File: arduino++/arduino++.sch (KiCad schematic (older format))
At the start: 23 parts, among them IC1 ATMEGA328PB-A, P1 CONN_01X18, P2 CONN_01X03, P3 USB_OTG, P4 CONN_01X03, P5 CONN_01X21, P6 CONN_01X03, P7 CONN_01X03, P8 CONN_02X03, Y1 Crystal

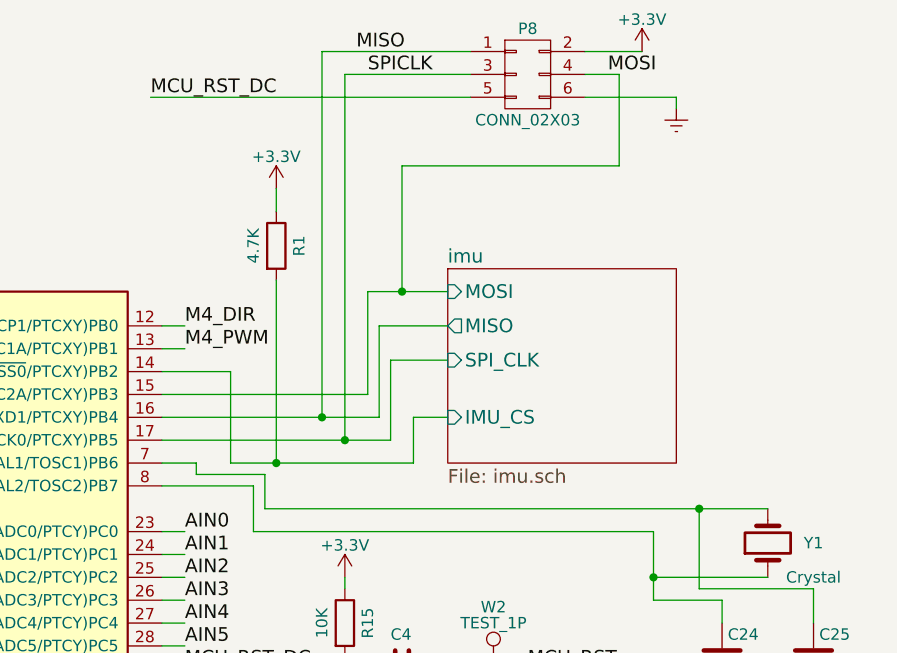
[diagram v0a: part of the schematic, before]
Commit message: Updating to latest rev as ordered on OSHPark.
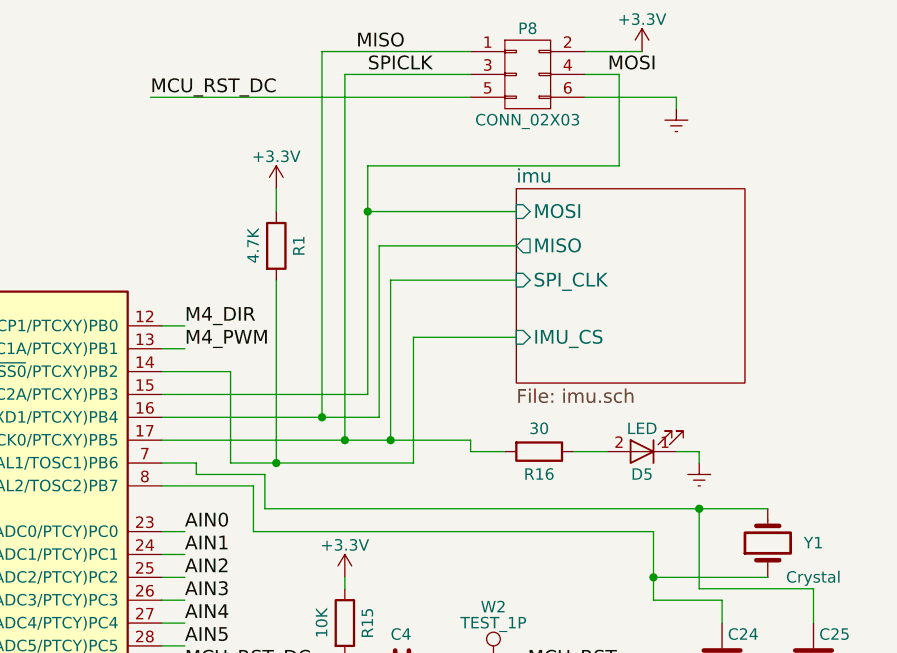
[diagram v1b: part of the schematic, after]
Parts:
- added D5: LED, LEDs:LED-0603, symbol LED
- added R16: 30, Resistors_SMD:R_0402, symbol R
- P3: manf# (none) -> 10118193-0001LF
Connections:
- net Earth: now also D5.1 (K)
- net SPICLK: now also R16.2
- new net: D5.2 (A), R16.1
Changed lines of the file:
@@
 F 2 "Connect:USB_Micro-B" H 4000 950 50  0001 C CNN
 F 3 "" V 4000 950 50  0000 C CNN
+F 4 "10118193-0001LF" H 4050 1050 60  0001 C CNN "manf#"
 	1    4050 1050
 	0    -1   -1   0
@@
 $EndComp
 $Comp
-L Earth #PWR01
+L Earth #PWR14
 U 1 1 582B5FCD
 P 4600 1500
-F 0 "#PWR01" H 4600 1250 50  0001 C CNN
+F 0 "#PWR14" H 4600 1250 50  0001 C CNN
 F 1 "Earth" H 4600 1350 50  0001 C CNN
 F 2 "" H 4600 1500 50  0000 C CNN
@@
 NoConn ~ 4350 950
 $Comp
-L Earth #PWR02
+L Earth #PWR16
 U 1 1 582B619C
 P 6000 5950
-F 0 "#PWR02" H 6000 5700 50  0001 C CNN
+F 0 "#PWR16" H 6000 5700 50  0001 C CNN
 F 1 "Earth" H 6000 5800 50  0001 C CNN
 F 2 "" H 6000 5950 50  0000 C CNN
@@
 $EndSheet
 $Sheet
-S 8700 2850 1000 850
+S 9000 2500 1000 850
 U 582C0B32
 F0 "imu" 60
 F1 "imu.sch" 60
-F2 "IMU_CS" I L 8700 3500 60
-F3 "SPI_CLK" I L 8700 3250 60
-F4 "MISO" O L 8700 3100 60
-F5 "MOSI" I L 8700 2950 60
+F2 "IMU_CS" I L 9000 3150 60
+F3 "SPI_CLK" I L 9000 2900 60
+F4 "MISO" O L 9000 2750 60
+F5 "MOSI" I L 9000 2600 60
 $EndSheet
 Text Label 7550 4000 0    60   ~ 0
@@
 $EndComp
 $Comp
-L Earth #PWR03
+L Earth #PWR13
 U 1 1 582C2BB8
 P 4550 3750
-F 0 "#PWR03" H 4550 3500 50  0001 C CNN
+F 0 "#PWR13" H 4550 3500 50  0001 C CNN
 F 1 "Earth" H 4550 3600 50  0001 C CNN
 F 2 "" H 4550 3750 50  0000 C CNN
@@
 M4_PWM
 $Comp
-L +3.3V #PWR04
+L +3.3V #PWR11
 U 1 1 582D1956
 P 3850 2650
-F 0 "#PWR04" H 3850 2500 50  0001 C CNN
+F 0 "#PWR11" H 3850 2500 50  0001 C CNN
 F 1 "+3.3V" H 3850 2790 50  0000 C CNN
 F 2 "" H 3850 2650 50  0000 C CNN
@@
 	4250 2950 4250 2950
 Wire Wire Line
-	7450 3600 8450 3600
+	7450 3600 8800 3600
 Wire Wire Line
 	7450 3500 8400 3500
 Wire Wire Line
-	7450 3400 8350 3400
+	8350 3400 7450 3400
 Wire Wire Line
 	7450 4000 7550 4000
@@
 Connection ~ 4550 3400
 Wire Wire Line
-	8350 3400 8350 2950
-Wire Wire Line
-	8350 2950 8700 2950
-Wire Wire Line
-	8400 3500 8400 3100
-Wire Wire Line
-	8400 3100 8700 3100
-Wire Wire Line
-	8450 3600 8450 3250
-Wire Wire Line
-	8450 3250 8700 3250
+	8350 2400 8350 3400
+Wire Wire Line
+	8350 2600 9000 2600
+Wire Wire Line
+	8400 3500 8400 2750
+Wire Wire Line
+	8400 2750 9000 2750
+Wire Wire Line
+	8450 3600 8450 2900
+Wire Wire Line
+	8450 2900 9000 2900
 Wire Wire Line
 	7750 3700 8550 3700
 Wire Wire Line
-	8550 3700 8550 3500
-Wire Wire Line
-	8550 3500 8700 3500
+	8550 3700 8550 3150
+Wire Wire Line
+	8550 3150 9000 3150
 Wire Wire Line
 	7950 3700 7950 2900
@@
 M4N
 $Comp
-L Earth #PWR05
+L Earth #PWR3
 U 1 1 58350D27
 P 1350 5150
-F 0 "#PWR05" H 1350 4900 50  0001 C CNN
+F 0 "#PWR3" H 1350 4900 50  0001 C CNN
 F 1 "Earth" H 1350 5000 50  0001 C CNN
 F 2 "" H 1350 5150 50  0000 C CNN
@@
 MCU_UART_TX
 $Comp
-L Earth #PWR06
+L Earth #PWR5
 U 1 1 58352CA7
 P 2600 5150
-F 0 "#PWR06" H 2600 4900 50  0001 C CNN
+F 0 "#PWR5" H 2600 4900 50  0001 C CNN
 F 1 "Earth" H 2600 5000 50  0001 C CNN
 F 2 "" H 2600 5150 50  0000 C CNN
@@
 M4_PWM
 $Comp
-L +3.3V #PWR07
+L +3.3V #PWR10
 U 1 1 5835EB7A
 P 3700 4950
-F 0 "#PWR07" H 3700 4800 50  0001 C CNN
+F 0 "#PWR10" H 3700 4800 50  0001 C CNN
 F 1 "+3.3V" H 3700 5090 50  0000 C CNN
 F 2 "" H 3700 4950 50  0000 C CNN
@@
 	7600 3700 7600 3750
 $Comp
-L +BATT #PWR08
+L +BATT #PWR4
 U 1 1 5836512B
 P 1700 4900
-F 0 "#PWR08" H 1700 4750 50  0001 C CNN
+F 0 "#PWR4" H 1700 4750 50  0001 C CNN
 F 1 "+BATT" H 1700 5040 50  0000 C CNN
 F 2 "" H 1700 4900 50  0000 C CNN
@@
 	3550 1350 4600 1350
 $Comp
-L PWR_FLAG #FLG09
+L PWR_FLAG #FLG1
 U 1 1 5836469D
 P 3550 1350
-F 0 "#FLG09" H 3550 1445 50  0001 C CNN
+F 0 "#FLG1" H 3550 1445 50  0001 C CNN
 F 1 "PWR_FLAG" H 3550 1530 50  0000 C CNN
 F 2 "" H 3550 1350 50  0000 C CNN
@@
 Connection ~ 8900 4600
 $Comp
-L +3.3V #PWR010
+L +3.3V #PWR17
 U 1 1 58A685D5
 P 7950 2500
-F 0 "#PWR010" H 7950 2350 50  0001 C CNN
+F 0 "#PWR17" H 7950 2350 50  0001 C CNN
 F 1 "+3.3V" H 7950 2640 50  0000 C CNN
 F 2 "" H 7950 2500 50  0000 C CNN
@@
 $EndComp
 $Comp
-L Earth #PWR011
+L Earth #PWR1
 U 1 1 58A6F427
 P 1200 6800
-F 0 "#PWR011" H 1200 6550 50  0001 C CNN
+F 0 "#PWR1" H 1200 6550 50  0001 C CNN
 F 1 "Earth" H 1200 6650 50  0001 C CNN
 F 2 "" H 1200 6800 50  0000 C CNN
@@
 $EndComp
 $Comp
-L Earth #PWR012
+L Earth #PWR2
 U 1 1 58A6F4FE
 P 1200 7450
-F 0 "#PWR012" H 1200 7200 50  0001 C CNN
+F 0 "#PWR2" H 1200 7200 50  0001 C CNN
 F 1 "Earth" H 1200 7300 50  0001 C CNN
 F 2 "" H 1200 7450 50  0000 C CNN
@@
 $EndComp
 $Comp
-L Earth #PWR013
+L Earth #PWR7
 U 1 1 58A6F5D5
 P 2700 7450
-F 0 "#PWR013" H 2700 7200 50  0001 C CNN
+F 0 "#PWR7" H 2700 7200 50  0001 C CNN
 F 1 "Earth" H 2700 7300 50  0001 C CNN
 F 2 "" H 2700 7450 50  0000 C CNN
@@
 $EndComp
 $Comp
-L Earth #PWR014
+L Earth #PWR6
 U 1 1 58A6F6AC
 P 2700 6800
-F 0 "#PWR014" H 2700 6550 50  0001 C CNN
+F 0 "#PWR6" H 2700 6550 50  0001 C CNN
 F 1 "Earth" H 2700 6650 50  0001 C CNN
 F 2 "" H 2700 6800 50  0000 C CNN
@@
 	2300 4750 2600 4750
 $Comp
-L +BATT #PWR015
+L +BATT #PWR8
 U 1 1 58A76494
 P 3450 4450
-F 0 "#PWR015" H 3450 4300 50  0001 C CNN
+F 0 "#PWR8" H 3450 4300 50  0001 C CNN
 F 1 "+BATT" H 3450 4590 50  0000 C CNN
 F 2 "" H 3450 4450 50  0000 C CNN
@@
 	2300 6100 2650 6100
 $Comp
-L Earth #PWR016
+L Earth #PWR12
 U 1 1 58A7C26F
 P 4450 3000
-F 0 "#PWR016" H 4450 2750 50  0001 C CNN
+F 0 "#PWR12" H 4450 2750 50  0001 C CNN
 F 1 "Earth" H 4450 2850 50  0001 C CNN
 F 2 "" H 4450 3000 50  0000 C CNN
@@
 Connection ~ 4450 3000
 $Comp
-L PWR_FLAG #FLG017
+L PWR_FLAG #FLG2
 U 1 1 58A83C22
 P 3900 5850
-F 0 "#FLG017" H 3900 5945 50  0001 C CNN
+F 0 "#FLG2" H 3900 5945 50  0001 C CNN
 F 1 "PWR_FLAG" H 3900 6030 50  0000 C CNN
 F 2 "" H 3900 5850 50  0000 C CNN
@@
 	7400 2100 8800 2100
 $Comp
-L +3.3V #PWR018
+L +3.3V #PWR19
 U 1 1 58A87135
 P 9550 1900
-F 0 "#PWR018" H 9550 1750 50  0001 C CNN
+F 0 "#PWR19" H 9550 1750 50  0001 C CNN
 F 1 "+3.3V" H 9550 2040 50  0000 C CNN
 F 2 "" H 9550 1900 50  0000 C CNN
@@
 	9300 1900 9550 1900
 Wire Wire Line
-	8500 2950 8500 2400
-Wire Wire Line
-	8500 2400 9450 2400
+	8350 2400 9450 2400
 Wire Wire Line
 	9450 2400 9450 2000
 Wire Wire Line
 	9450 2000 9300 2000
-Connection ~ 8500 2950
-$Comp
-L Earth #PWR019
+Connection ~ 8350 2600
+$Comp
+L Earth #PWR20
 U 1 1 58A879D1
 P 9700 2150
-F 0 "#PWR019" H 9700 1900 50  0001 C CNN
+F 0 "#PWR20" H 9700 1900 50  0001 C CNN
 F 1 "Earth" H 9700 2000 50  0001 C CNN
 F 2 "" H 9700 2150 50  0000 C CNN
@@
 	9900 4700 10300 4700
 $Comp
-L Earth #PWR020
+L Earth #PWR22
 U 1 1 58A8ACAB
 P 10100 4800
-F 0 "#PWR020" H 10100 4550 50  0001 C CNN
+F 0 "#PWR22" H 10100 4550 50  0001 C CNN
 F 1 "Earth" H 10100 4650 50  0001 C CNN
 F 2 "" H 10100 4800 50  0000 C CNN
@@
 	7850 4000 9600 4000
 $Comp
-L +3.3V #PWR021
+L +3.3V #PWR18
 U 1 1 58A8BF3F
 P 8250 4200
-F 0 "#PWR021" H 8250 4050 50  0001 C CNN
+F 0 "#PWR18" H 8250 4050 50  0001 C CNN
 F 1 "+3.3V" H 8250 4340 50  0000 C CNN
 F 2 "" H 8250 4200 50  0000 C CNN
@@
 	2300 3050 2600 3050
 $Comp
-L +3.3V #PWR022
+L +3.3V #PWR9
 U 1 1 58AACF83
 P 3600 4600
-F 0 "#PWR022" H 3600 4450 50  0001 C CNN
+F 0 "#PWR9" H 3600 4450 50  0001 C CNN
 F 1 "+3.3V" H 3600 4740 50  0000 C CNN
 F 2 "" H 3600 4600 50  0000 C CNN
@@
 $EndComp
 $Comp
-L Earth #PWR023
+L Earth #PWR15
 U 1 1 58B0080A
 P 5600 7250
-F 0 "#PWR023" H 5600 7000 50  0001 C CNN
+F 0 "#PWR15" H 5600 7000 50  0001 C CNN
 F 1 "Earth" H 5600 7100 50  0001 C CNN
 F 2 "" H 5600 7250 50  0000 C CNN
@@
 	1    0    0    -1
 $EndComp
+$Comp
+L LED D5
+U 1 1 58B45684
+P 9550 3650
+F 0 "D5" H 9550 3750 50  0000 C CNN
+F 1 "LED" H 9550 3550 50  0000 C CNN
+F 2 "LEDs:LED-0603" H 9550 3650 50  0001 C CNN
+F 3 "" H 9550 3650 50  0000 C CNN
+F 4 "LTST-C191KGKT" H 9550 3650 60  0001 C CNN "manf#"
+	1    9550 3650
+	-1   0    0    1
+$EndComp
+Wire Wire Line
+	8800 3600 8800 3650
+Connection ~ 8450 3600
+$Comp
+L Earth #PWR21
+U 1 1 58B459C5
+P 9800 3700
+F 0 "#PWR21" H 9800 3450 50  0001 C CNN
+F 1 "Earth" H 9800 3550 50  0001 C CNN
+F 2 "" H 9800 3700 50  0000 C CNN
+F 3 "" H 9800 3700 50  0000 C CNN
+	1    9800 3700
+	1    0    0    -1
+$EndComp
+Wire Wire Line
+	9700 3650 9800 3650
+Wire Wire Line
+	9800 3650 9800 3700
+$Comp
+L R R16
+U 1 1 58B45ED9
+P 9100 3650
+F 0 "R16" V 9200 3650 50  0000 C CNN
+F 1 "30" V 9000 3650 50  0000 C CNN
+F 2 "Resistors_SMD:R_0402" H 9030 3650 50  0001 C CNN
+F 3 "" H 9100 3650 50  0000 C CNN
+F 4 "RC0402JR-0730RL" V 9100 3650 60  0001 C CNN "manf#"
+	1    9100 3650
+	0    1    1    0
+$EndComp
+Wire Wire Line
+	8800 3650 8950 3650
+Wire Wire Line
+	9250 3650 9400 3650
 $EndSCHEMATC
